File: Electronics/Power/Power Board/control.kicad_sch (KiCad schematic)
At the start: 45 parts, among them IC1 STM32U575VGT6, IC302 TJA1057GT/3, J1 TYPE-C-31-M-12, J3 TC2030, J303 Screw_Terminal_01x03, SW301 SW_DIP_x02, U1 USBLC6-4SC6-ES, U2 USBLC6-4SC6-ES, U303 TVS1800DRV, X301 25MHz_Clock, X302 32.768kHz_Clock

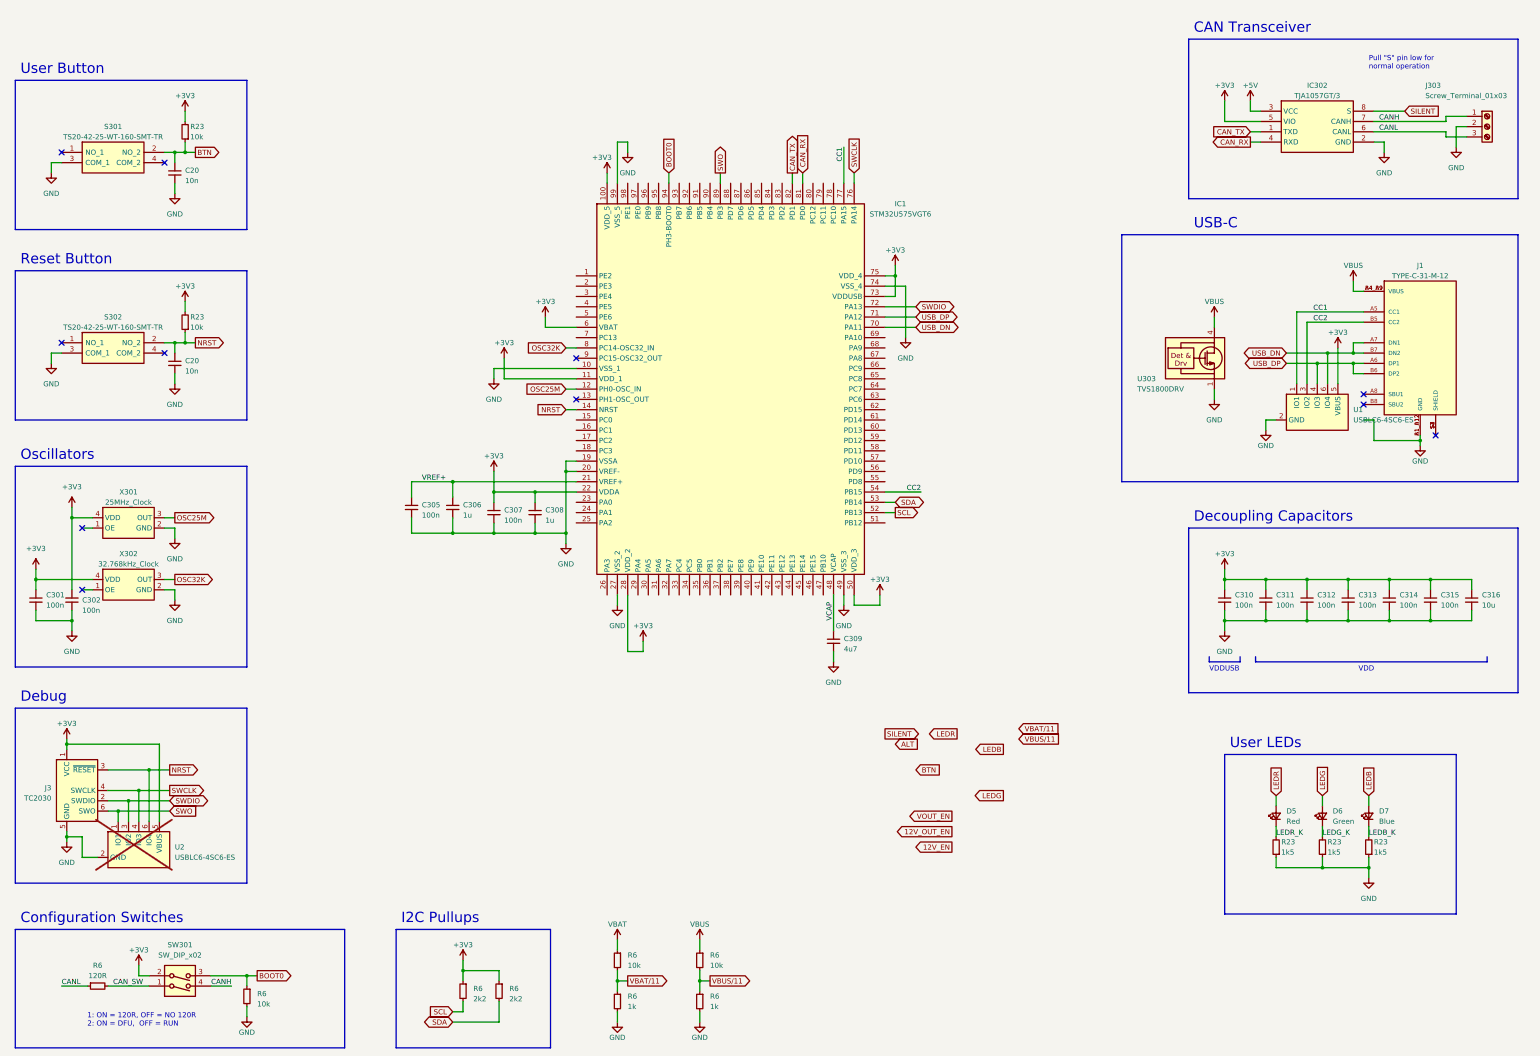
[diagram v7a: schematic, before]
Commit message: Gateway board layout complete and routing begun
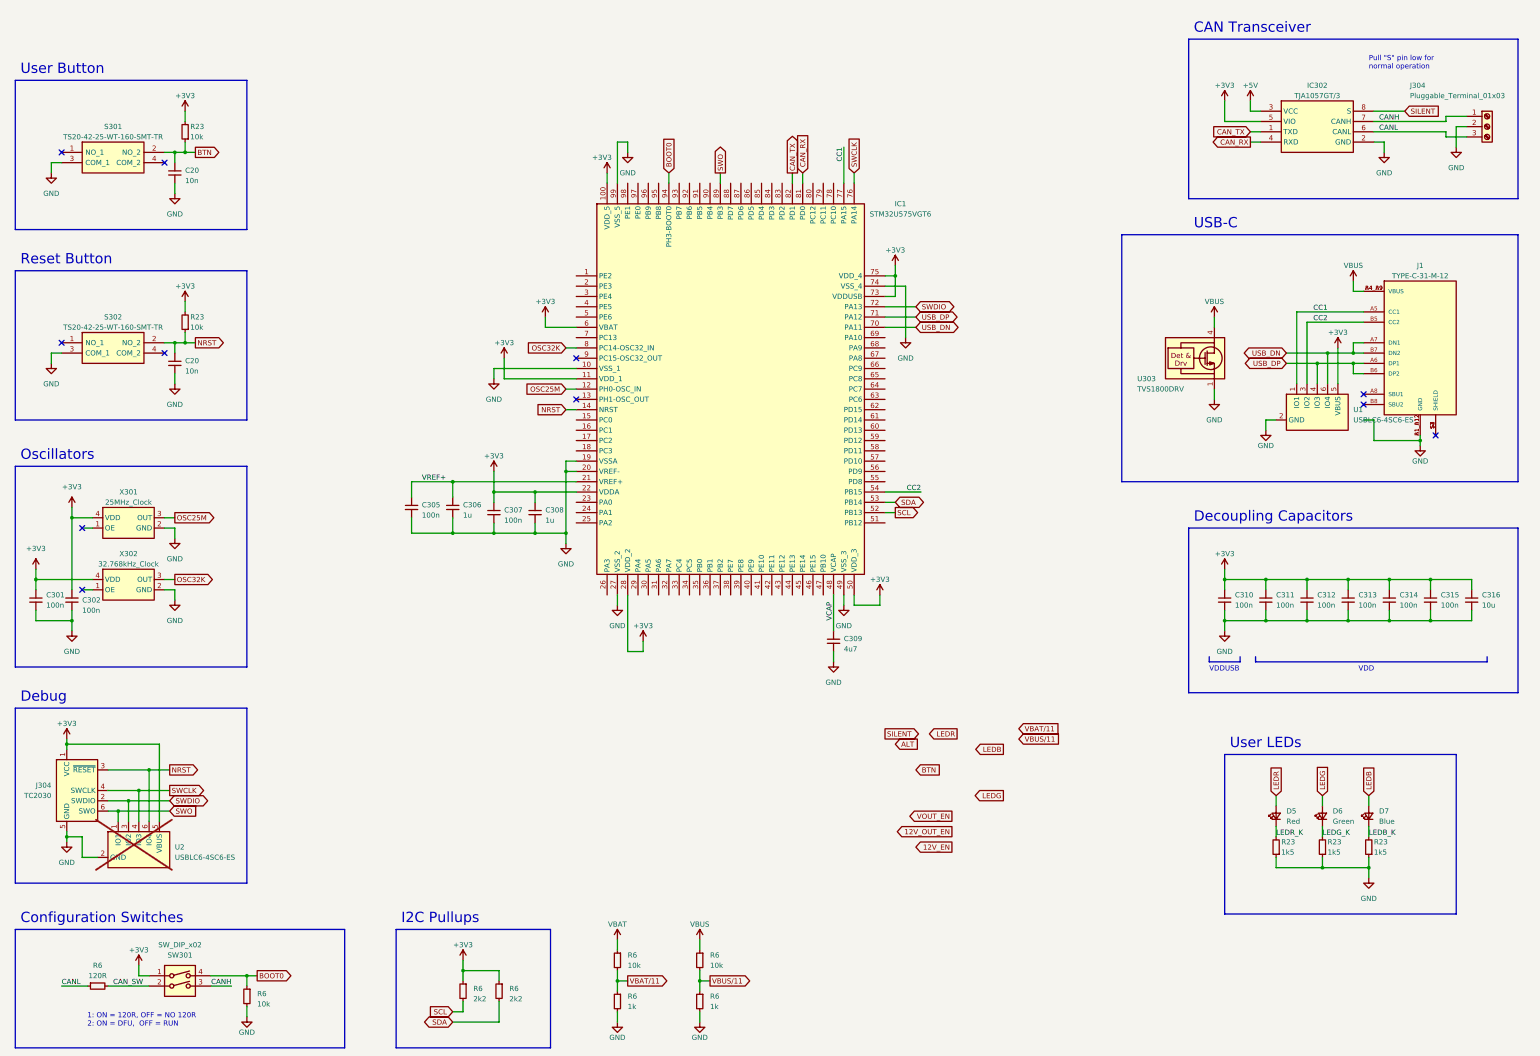
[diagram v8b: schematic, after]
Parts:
- removed J3: TC2030, Connector:Tag-Connect_TC2030-IDC-FP_2x03_P1.27mm_Vertical, symbol Connector:Conn_ARM_SWD_TagConnect_TC2030
- removed J303: Screw_Terminal_01x03, TerminalBlock:TerminalBlock_bornier-3_P5.08mm, symbol Connector:Screw_Terminal_01x03
- added J304: TC2030, MSL Footprints:Tag-Connect_TC2030-IDC-FP_2x03_P1.27mm_Vertical, symbol MSL_Symbols:TC2030
- added J304: Pluggable_Terminal_01x03, MSL Footprints:Pluggable_terminal-3_P5.08mm, symbol MSL_Symbols:Pluggable_Terminal_01x03
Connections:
- net +3V3: now also SW301.1, J304.1 (VCC); no longer SW301.2
- net BOOT0: now also SW301.4; no longer SW301.3
- net CANH: now also SW301.3, J304.1 (Pin_1); no longer SW301.4
- net CANL: now also J304.3 (Pin_3)
- net CAN_SW: now also SW301.2; no longer SW301.1
- net GND: now also J304.2 (Pin_2), J304.5 (GND)
- net NRST: now also J304.3 (~{RESET})
- net SWCLK: now also J304.4 (SWCLK)
- net SWDIO: now also J304.2 (SWDIO)
- net SWO: now also J304.6 (SWO)
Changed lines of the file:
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@@
     (stroke (width 0) (type default))
   )
+  (wire (pts (xy 34.29 203.2) (xy 34.29 201.93))
+    (stroke (width 0) (type default))
+  )
   (wire (pts (xy 238.76 142.24) (xy 236.22 142.24))
     (stroke (width 0) (type default))
@@
     (stroke (width 0) (type default))
   )
-  (wire (pts (xy 34.29 201.93) (xy 34.29 203.2))
-    (stroke (width 0) (type default))
-  )
   (wire (pts (xy 34.29 201.93) (xy 57.15 201.93))
     (stroke (width 0) (type default))
@@
     )
   )
-  (symbol (lib_id "Connector:Screw_Terminal_01x03") (at 384.81 49.53 0) (unit 1)
-    (in_bom yes) (on_board yes) (dnp no)
-    (property "Reference" "J303" (at 369.57 39.37 0)
-      (effects (font (size 1.27 1.27)) (justify left))
-    )
-    (property "Value" "Screw_Terminal_01x03" (at 369.57 41.91 0)
-      (effects (font (size 1.27 1.27)) (justify left))
-    )
-    (property "Footprint" "TerminalBlock:TerminalBlock_bornier-3_P5.08mm" (at 384.81 49.53 0)
-      (effects (font (size 1.27 1.27)) hide)
-    )
-    (property "Datasheet" "~" (at 384.81 49.53 0)
-      (effects (font (size 1.27 1.27)) hide)
-    )
-    (pin "1")
-    (pin "2")
-    (pin "3")
-    (instances
-      (project "Power Board"
-        (path "/d8843e0a-fd8a-4193-ba57-f0164156e030/fab43204-4de8-48e9-a4c9-80bcd4a9c27a"
-          (reference "J303") (unit 1)
-        )
-      )
-    )
-  )
   (symbol (lib_id "power:+3V3") (at 52.07 256.54 0) (unit 1)
     (in_bom yes) (on_board yes) (dnp no) (fields_autoplaced)
@@
     )
   )
+  (symbol (lib_id "MSL_Symbols:TC2030") (at 36.83 213.36 0) (unit 1)
+    (in_bom no) (on_board yes) (dnp no)
+    (property "Reference" "J304" (at 30.48 212.09 0)
+      (effects (font (size 1.27 1.27)) (justify right))
+    )
+    (property "Value" "TC2030" (at 30.48 214.63 0)
+      (effects (font (size 1.27 1.27)) (justify right))
+    )
+    (property "Footprint" "MSL Footprints:Tag-Connect_TC2030-IDC-FP_2x03_P1.27mm_Vertical" (at 36.83 231.14 0)
+      (effects (font (size 1.27 1.27)) hide)
+    )
+    (property "Datasheet" "https://www.tag-connect.com/wp-content/uploads/bsk-pdf-manager/TC2030-CTX_1.pdf" (at 36.83 228.6 0)
+      (effects (font (size 1.27 1.27)) hide)
+    )
+    (pin "1")
+    (pin "2")
+    (pin "3")
+    (pin "4")
+    (pin "5")
+    (pin "6")
+    (instances
+      (project "Motor Driver Board"
+        (path "/5318664d-e328-4e84-a383-7318275dc447/86a04d6c-5487-4291-b767-6da69e96f7da"
+          (reference "J304") (unit 1)
+        )
+      )
+      (project "Power Board"
+        (path "/d8843e0a-fd8a-4193-ba57-f0164156e030/fab43204-4de8-48e9-a4c9-80bcd4a9c27a"
+          (reference "J301") (unit 1)
+        )
+      )
+    )
+  )
   (symbol (lib_id "Device:C_Small") (at 60.96 107.95 0) (unit 1)
     (in_bom yes) (on_board yes) (dnp no) (fields_autoplaced)
@@
     )
   )
-  (symbol (lib_id "power:+3V3") (at 347.98 104.14 0) (unit 1)
-    (in_bom yes) (on_board yes) (dnp no) (fields_autoplaced)
-    (property "Reference" "#PWR0336" (at 347.98 107.95 0)
-      (effects (font (size 1.27 1.27)) hide)
+  (symbol (lib_id "Switch:SW_DIP_x02") (at 62.23 261.62 0) (unit 1)
+    (in_bom yes) (on_board yes) (dnp no)
+    (property "Reference" "SW301" (at 62.23 254 0)
+      (effects (font (size 1.27 1.27)))
     )
-    (property "Value" "+3V3" (at 347.98 100.33 0)
+    (property "Value" "SW_DIP_x02" (at 62.23 251.46 0)
       (effects (font (size 1.27 1.27)))
     )
-    (property "Footprint" "" (at 347.98 104.14 0)
+    (property "Footprint" "Package_DIP:DIP-4_W8.89mm_SMDSocket_LongPads" (at 62.23 261.62 0)
       (effects (font (size 1.27 1.27)) hide)
     )
-    (property "Datasheet" "" (at 347.98 104.14 0)
+    (property "Datasheet" "~" (at 62.23 261.62 0)
       (effects (font (size 1.27 1.27)) hide)
     )
     (pin "1")
+    (pin "2")
+    (pin "3")
+    (pin "4")
     (instances
       (project "Power Board"
         (path "/d8843e0a-fd8a-4193-ba57-f0164156e030/fab43204-4de8-48e9-a4c9-80bcd4a9c27a"
-          (reference "#PWR0336") (unit 1)
+          (reference "SW301") (unit 1)
         )
       )
     )
   )
-  (symbol (lib_id "Switch:SW_DIP_x02") (at 62.23 259.08 0) (mirror x) (unit 1)
-    (in_bom yes) (on_board yes) (dnp no)
-    (property "Reference" "SW301" (at 62.23 251.46 0)
-      (effects (font (size 1.27 1.27)))
+  (symbol (lib_id "power:+3V3") (at 347.98 104.14 0) (unit 1)
+    (in_bom yes) (on_board yes) (dnp no) (fields_autoplaced)
+    (property "Reference" "#PWR0336" (at 347.98 107.95 0)
+      (effects (font (size 1.27 1.27)) hide)
     )
-    (property "Value" "SW_DIP_x02" (at 62.23 254 0)
+    (property "Value" "+3V3" (at 347.98 100.33 0)
       (effects (font (size 1.27 1.27)))
     )
-    (property "Footprint" "Package_DIP:DIP-4_W8.89mm_SMDSocket_LongPads" (at 62.23 259.08 0)
+    (property "Footprint" "" (at 347.98 104.14 0)
       (effects (font (size 1.27 1.27)) hide)
     )
-    (property "Datasheet" "~" (at 62.23 259.08 0)
+    (property "Datasheet" "" (at 347.98 104.14 0)
       (effects (font (size 1.27 1.27)) hide)
     )
     (pin "1")
-    (pin "2")
-    (pin "3")
-    (pin "4")
     (instances
       (project "Power Board"
         (path "/d8843e0a-fd8a-4193-ba57-f0164156e030/fab43204-4de8-48e9-a4c9-80bcd4a9c27a"
-          (reference "SW301") (unit 1)
+          (reference "#PWR0336") (unit 1)
         )
       )
@@
     )
   )
+  (symbol (lib_id "MSL_Symbols:Pluggable_Terminal_01x03") (at 384.81 49.53 0) (unit 1)
+    (in_bom yes) (on_board yes) (dnp no)
+    (property "Reference" "J304" (at 365.76 39.37 0)
+      (effects (font (size 1.27 1.27)) (justify left))
+    )
+    (property "Value" "Pluggable_Terminal_01x03" (at 365.76 41.91 0)
+      (effects (font (size 1.27 1.27)) (justify left))
+    )
+    (property "Footprint" "MSL Footprints:Pluggable_terminal-3_P5.08mm" (at 384.81 49.53 0)
+      (effects (font (size 1.27 1.27)) hide)
+    )
+    (property "Datasheet" "~" (at 384.81 49.53 0)
+      (effects (font (size 1.27 1.27)) hide)
+    )
+    (pin "1")
+    (pin "2")
+    (pin "3")
+    (instances
+      (project "Gateway Board"
+        (path "/5318664d-e328-4e84-a383-7318275dc447/86a04d6c-5487-4291-b767-6da69e96f7da"
+          (reference "J304") (unit 1)
+        )
+      )
+      (project "Power Board"
+        (path "/d8843e0a-fd8a-4193-ba57-f0164156e030/fab43204-4de8-48e9-a4c9-80bcd4a9c27a"
+          (reference "J303") (unit 1)
+        )
+      )
+    )
+  )
   (symbol (lib_id "power:+3V3") (at 320.04 158.75 0) (unit 1)
     (in_bom yes) (on_board yes) (dnp no) (fields_autoplaced)
@@
         )
       )
-    )
-  )
-  (symbol (lib_id "Connector:Conn_ARM_SWD_TagConnect_TC2030") (at 36.83 213.36 0) (unit 1)
-    (in_bom no) (on_board yes) (dnp no) (fields_autoplaced)
-    (property "Reference" "J3" (at 30.48 212.725 0)
-      (effects (font (size 1.27 1.27)) (justify right))
-    )
-    (property "Value" "TC2030" (at 30.48 215.265 0)
-      (effects (font (size 1.27 1.27)) (justify right))
-    )
-    (property "Footprint" "Connector:Tag-Connect_TC2030-IDC-FP_2x03_P1.27mm_Vertical" (at 36.83 231.14 0)
-      (effects (font (size 1.27 1.27)) hide)
-    )
-    (property "Datasheet" "https://www.tag-connect.com/wp-content/uploads/bsk-pdf-manager/TC2030-CTX_1.pdf" (at 36.83 228.6 0)
-      (effects (font (size 1.27 1.27)) hide)
-    )
-    (pin "1")
-    (pin "2")
-    (pin "3")
-    (pin "4")
-    (pin "5")
-    (pin "6")
-    (instances
-      (project "Gateway Board"
-        (path "/5318664d-e328-4e84-a383-7318275dc447/86a04d6c-5487-4291-b767-6da69e96f7da"
-          (reference "J3") (unit 1)
-        )
-      )
-      (project "Power Board"
-        (path "/d8843e0a-fd8a-4193-ba57-f0164156e030/fab43204-4de8-48e9-a4c9-80bcd4a9c27a"
-          (reference "J301") (unit 1)
-        )
-      )
